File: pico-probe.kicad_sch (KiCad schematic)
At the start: 36 parts, among them J1 Conn_01x04, J2 USB_C_Receptacle_USB2.0, J3 Conn_01x05, SW1 SW_Push, U1 RP2040, U3 USBLC6-4SC6, U4 SPX1117-3.3, U5 W25Q16JVSS, Y1 Crystal_GND24

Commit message: 布线
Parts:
- added D2, D5: ESD5341, KisonNew:esd5341, symbol KisonNew:ESD5341
- C12, C13: LCSC C1648 -> C1554
- C15, C16: footprint Capacitor_SMD:C_0805_2012Metric -> Capacitor_SMD:C_0603_1608Metric; LCSC C15850 -> C19702; Price 0.08 -> 0.04
- C3, C5: LCSC C15849 -> C52923
- R3, R5: LCSC (none) -> C11702
- R6, R7: LCSC C325524 -> C25905
- Y1: LCSC (none) -> C9002
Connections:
- net EXT_5V is gone; now on net +5V: JP1.3 (B)
- net GND: now also D2.2 (A2), D5.2 (A2)
- net GPIO4: now also D5.1 (A1)
- net GPIO5: now also D2.1 (A1)
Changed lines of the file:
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@@
+    (effects (font (size 1.27 1.27)) (justify right bottom))
+  )
+  (label "TX" (at 221.234 120.396 180)
     (effects (font (size 1.27 1.27)) (justify right bottom))
   )
@@
     (effects (font (size 1.27 1.27)) (justify right bottom))
   )
+  (label "VSYS" (at 230.378 148.971 0)
+    (effects (font (size 1.27 1.27)) (justify left bottom))
+  )
   (label "GPIO18" (at 143.129 118.745 180)
     (effects (font (size 1.27 1.27)) (justify right bottom))
@@
   (label "GPIO12" (at 143.129 103.505 180)
     (effects (font (size 1.27 1.27)) (justify right bottom))
-  )
-  (label "EXT_5V" (at 230.378 148.971 0)
-    (effects (font (size 1.27 1.27)) (justify left bottom))
   )
   (label "QSPI_SD3" (at 281.051 100.203 180)
@@
   )
   (label "GPIO6" (at 143.129 88.265 180)
+    (effects (font (size 1.27 1.27)) (justify right bottom))
+  )
+  (label "RX" (at 221.615 129.286 180)
     (effects (font (size 1.27 1.27)) (justify right bottom))
   )
@@
       (effects (font (size 1.27 1.27)) (justify left))
     )
-    (property "Footprint" "Capacitor_SMD:C_0805_2012Metric" (id 2) (at 59.9948 187.96 0)
+    (property "Footprint" "Capacitor_SMD:C_0603_1608Metric" (id 2) (at 59.9948 187.96 0)
       (effects (font (size 1.27 1.27)) hide)
     )
@@
       (effects (font (size 1.27 1.27)) hide)
     )
-    (property "LCSC" "C15850" (id 4) (at 60.96 184.15 0)
-      (effects (font (size 1.27 1.27)) hide)
-    )
-    (property "Price" "0.08" (id 5) (at 60.96 184.15 0)
+    (property "LCSC" "C19702" (id 4) (at 60.96 184.15 0)
+      (effects (font (size 1.27 1.27)) hide)
+    )
+    (property "Price" "0.04" (id 5) (at 60.96 184.15 0)
       (effects (font (size 1.27 1.27)) hide)
     )
@@
       (effects (font (size 1.27 1.27)) hide)
     )
+    (property "LCSC" "C11702" (id 4) (at 257.429 41.529 0)
+      (effects (font (size 1.27 1.27)) hide)
+    )
     (pin "1")
     (pin "2")
@@
     )
     (property "Datasheet" "~" (id 3) (at 221.361 92.583 0)
+      (effects (font (size 1.27 1.27)) hide)
+    )
+    (property "LCSC" "C11702" (id 4) (at 221.361 92.583 0)
       (effects (font (size 1.27 1.27)) hide)
     )
@@
       (effects (font (size 1.27 1.27)) hide)
     )
-    (property "LCSC" "C1648" (id 4) (at 224.409 41.529 0)
+    (property "LCSC" "C1554" (id 4) (at 224.409 41.529 0)
       (effects (font (size 1.27 1.27)) hide)
     )
@@
     (pin "1")
   )
+  (symbol (lib_id "power:GND") (at 229.235 129.286 90) (unit 1)
+    (in_bom yes) (on_board yes) (fields_autoplaced)
+    (property "Reference" "#PWR0119" (id 0) (at 235.585 129.286 0)
+      (effects (font (size 1.27 1.27)) hide)
+    )
+    (property "Value" "GND" (id 1) (at 232.41 129.7198 90)
+      (effects (font (size 1.27 1.27)) (justify right))
+    )
+    (property "Footprint" "" (id 2) (at 229.235 129.286 0)
+      (effects (font (size 1.27 1.27)) hide)
+    )
+    (property "Datasheet" "" (id 3) (at 229.235 129.286 0)
+      (effects (font (size 1.27 1.27)) hide)
+    )
+    (pin "1")
+  )
+  (symbol (lib_id "power:GND") (at 228.854 120.396 90) (unit 1)
+    (in_bom yes) (on_board yes) (fields_autoplaced)
+    (property "Reference" "#PWR0118" (id 0) (at 235.204 120.396 0)
+      (effects (font (size 1.27 1.27)) hide)
+    )
+    (property "Value" "GND" (id 1) (at 232.029 120.8298 90)
+      (effects (font (size 1.27 1.27)) (justify right))
+    )
+    (property "Footprint" "" (id 2) (at 228.854 120.396 0)
+      (effects (font (size 1.27 1.27)) hide)
+    )
+    (property "Datasheet" "" (id 3) (at 228.854 120.396 0)
+      (effects (font (size 1.27 1.27)) hide)
+    )
+    (pin "1")
+  )
   (symbol (lib_id "Device:C") (at 121.539 42.545 0) (unit 1)
     (in_bom yes) (on_board yes)
@@
       (effects (font (size 1.27 1.27)) hide)
     )
-    (property "LCSC" "C15849" (id 4) (at 121.539 42.545 0)
+    (property "LCSC" "C52923" (id 4) (at 121.539 42.545 0)
       (effects (font (size 1.27 1.27)) hide)
     )
@@
       (effects (font (size 1.27 1.27)) hide)
     )
+    (property "LCSC" "C9002" (id 4) (at 239.649 36.449 0)
+      (effects (font (size 1.27 1.27)) hide)
+    )
     (pin "1")
     (pin "2")
@@
       (effects (font (size 1.27 1.27)) hide)
     )
-    (property "LCSC" "C15849" (id 4) (at 66.929 42.545 0)
+    (property "LCSC" "C52923" (id 4) (at 66.929 42.545 0)
       (effects (font (size 1.27 1.27)) hide)
     )
@@
       (effects (font (size 1.27 1.27)) hide)
     )
-    (property "LCSC" "C1648" (id 4) (at 224.409 31.369 0)
+    (property "LCSC" "C1554" (id 4) (at 224.409 31.369 0)
       (effects (font (size 1.27 1.27)) hide)
     )
@@
       (effects (font (size 1.27 1.27)) hide)
     )
-    (property "LCSC" "C325524" (id 4) (at 45.72 161.544 0)
+    (property "LCSC" "C25905" (id 4) (at 45.72 161.544 0)
       (effects (font (size 1.27 1.27)) hide)
     )
@@
       (effects (font (size 1.27 1.27)) hide)
     )
-    (property "LCSC" "C325524" (id 4) (at 45.72 159.004 0)
+    (property "LCSC" "C25905" (id 4) (at 45.72 159.004 0)
       (effects (font (size 1.27 1.27)) hide)
     )
@@
     )
     (pin "1")
+  )
+  (symbol (lib_id "KisonNew:ESD5341") (at 225.425 129.286 0) (unit 1)
+    (in_bom yes) (on_board yes) (fields_autoplaced)
+    (property "Reference" "D5" (id 0) (at 225.4885 124.3416 0))
+    (property "Value" "ESD5341" (id 1) (at 225.4885 126.8785 0))
+    (property "Footprint" "KisonNew:esd5341" (id 2) (at 225.425 122.936 0)
+      (effects (font (size 1.27 1.27)) hide)
+    )
+    (property "Datasheet" "" (id 3) (at 226.695 124.206 0)
+      (effects (font (size 1.27 1.27)) hide)
+    )
+    (property "LCSC" "C239773" (id 4) (at 225.425 129.286 0)
+      (effects (font (size 1.27 1.27)) hide)
+    )
+    (property "Price" "0.2" (id 5) (at 225.425 129.286 0)
+      (effects (font (size 1.27 1.27)) hide)
+    )
+    (pin "1")
+    (pin "2")
   )
   (symbol (lib_id "power:GND") (at 194.691 92.583 0) (unit 1)
@@
     (pin "1")
   )
+  (symbol (lib_id "KisonNew:ESD5341") (at 225.044 120.396 0) (unit 1)
+    (in_bom yes) (on_board yes) (fields_autoplaced)
+    (property "Reference" "D2" (id 0) (at 225.1075 115.4516 0))
+    (property "Value" "ESD5341" (id 1) (at 225.1075 117.9885 0))
+    (property "Footprint" "KisonNew:esd5341" (id 2) (at 225.044 114.046 0)
+      (effects (font (size 1.27 1.27)) hide)
+    )
+    (property "Datasheet" "" (id 3) (at 226.314 115.316 0)
+      (effects (font (size 1.27 1.27)) hide)
+    )
+    (property "LCSC" "C239773" (id 4) (at 225.044 120.396 0)
+      (effects (font (size 1.27 1.27)) hide)
+    )
+    (property "Price" "0.2" (id 5) (at 225.044 120.396 0)
+      (effects (font (size 1.27 1.27)) hide)
+    )
+    (pin "1")
+    (pin "2")
+  )
   (symbol (lib_id "power:+1V1") (at 75.819 20.955 0) (unit 1)
     (in_bom yes) (on_board yes)
@@
       (effects (font (size 1.27 1.27)) (justify left))
     )
-    (property "Footprint" "Capacitor_SMD:C_0805_2012Metric" (id 2) (at 77.1652 187.96 0)
+    (property "Footprint" "Capacitor_SMD:C_0603_1608Metric" (id 2) (at 77.1652 187.96 0)
       (effects (font (size 1.27 1.27)) hide)
     )
@@
       (effects (font (size 1.27 1.27)) hide)
     )
-    (property "LCSC" "C15850" (id 4) (at 76.2 184.15 0)
-      (effects (font (size 1.27 1.27)) hide)
-    )
-    (property "Price" "0.08" (id 5) (at 76.2 184.15 0)
+    (property "LCSC" "C19702" (id 4) (at 76.2 184.15 0)
+      (effects (font (size 1.27 1.27)) hide)
+    )
+    (property "Price" "0.04" (id 5) (at 76.2 184.15 0)
       (effects (font (size 1.27 1.27)) hide)
     )
@@
       (reference "#PWR0117") (unit 1) (value "GND") (footprint "")
     )
+    (path "/5be2a7ef-6d75-469c-9372-d3ffb1deb597"
+      (reference "#PWR0118") (unit 1) (value "GND") (footprint "")
+    )
+    (path "/5b45f8dc-bdc9-483f-a370-b95cb3c66794"
+      (reference "#PWR0119") (unit 1) (value "GND") (footprint "")
+    )
     (path "/775ab88d-bcfe-4114-9420-f4fd8ff148c3"
       (reference "#PWR0120") (unit 1) (value "GND") (footprint "")
@@
     )
     (path "/0516868f-abb8-4b83-8e2d-2d322e9f7b87"
-      (reference "C15") (unit 1) (value "10uf") (footprint "Capacitor_SMD:C_0805_2012Metric")
+      (reference "C15") (unit 1) (value "10uf") (footprint "Capacitor_SMD:C_0603_1608Metric")
     )
     (path "/f8ea8509-0869-4765-a579-07b13d0cb0fd"
-      (reference "C16") (unit 1) (value "10uf") (footprint "Capacitor_SMD:C_0805_2012Metric")
+      (reference "C16") (unit 1) (value "10uf") (footprint "Capacitor_SMD:C_0603_1608Metric")
     )
     (path "/99fe2f6d-1f82-4f84-a150-a09d92a8f576"
       (reference "D1") (unit 1) (value "D") (footprint "KisonNew:C8678")
     )
+    (path "/df9c2dea-53d2-468a-b74a-d1daef510987"
+      (reference "D2") (unit 1) (value "ESD5341") (footprint "KisonNew:esd5341")
+    )
     (path "/54bc26a8-1258-45ab-b9ed-89a95631aa30"
       (reference "D3") (unit 1) (value "ESD5341") (footprint "KisonNew:esd5341")
@@
       (reference "D4") (unit 1) (value "ESD5341") (footprint "KisonNew:esd5341")
     )
+    (path "/c2152c92-14f4-4079-9d64-d37e9be7e0d9"
+      (reference "D5") (unit 1) (value "ESD5341") (footprint "KisonNew:esd5341")
+    )
     (path "/6c900b51-bd89-4dac-8fad-0aea210c3a6d"

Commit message: 新布线
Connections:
- net DeviceVcc: now also J3.1 (Pin_1)
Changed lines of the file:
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@@
+    (effects (font (size 1.27 1.27)) (justify right bottom))
+  )
+  (label "DeviceVcc" (at 178.308 124.587 180)
     (effects (font (size 1.27 1.27)) (justify right bottom))
   )

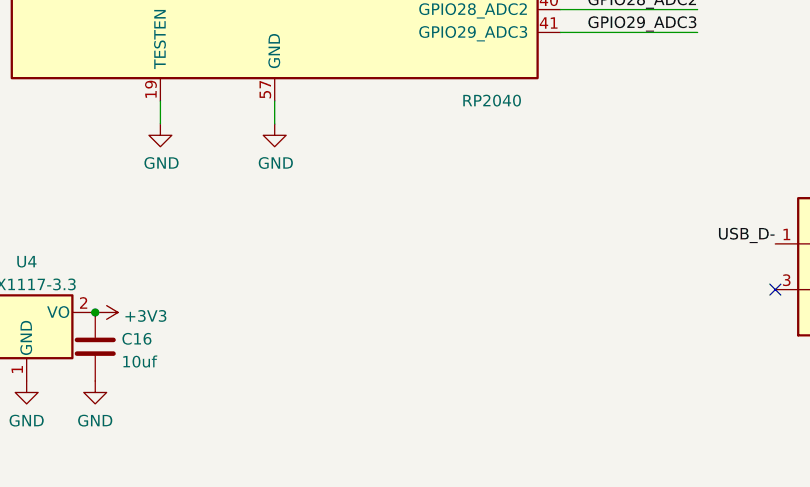
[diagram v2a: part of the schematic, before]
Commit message: 添加LED
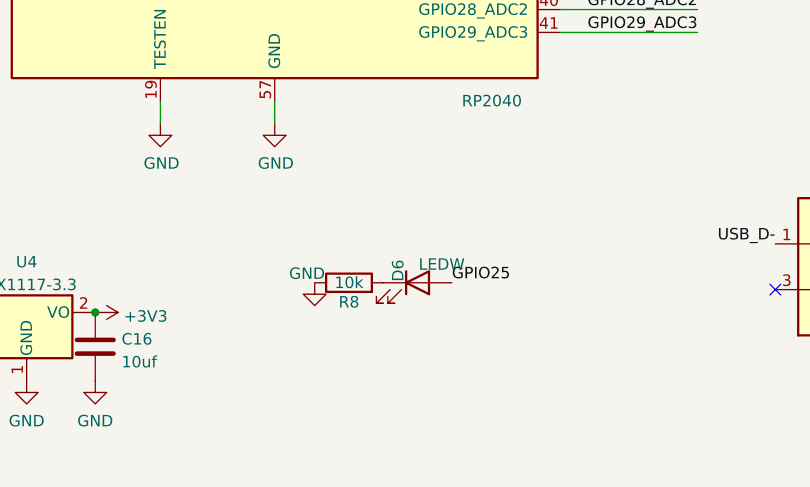
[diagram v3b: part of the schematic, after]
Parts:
- added D6: LEDW, LED_SMD:LED_0603_1608Metric, symbol Device:LED
- added R8: 10k, Resistor_SMD:R_0402_1005Metric, symbol Device:R
- C15, C16: Price 0.04 -> (none)
- D2, D3, D4, D5: Price 0.2 -> (none)
- U4: Price 0.76 -> (none)
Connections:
- net GND: now also R8.1
- net GPIO25: now also D6.2 (A)
- new net: D6.1 (K), R8.2
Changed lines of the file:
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@@
     (effects (font (size 1.27 1.27)) (justify right bottom))
+  )
+  (label "GPIO25" (at 115.824 177.038 0)
+    (effects (font (size 1.27 1.27)) (justify left bottom))
   )
   (label "SWD" (at 50.419 140.335 0)
@@
       (effects (font (size 1.27 1.27)) hide)
     )
-    (property "Price" "0.2" (id 5) (at 179.451 150.114 0)
+    (property "Price" "" (id 5) (at 179.451 150.114 0)
       (effects (font (size 1.27 1.27)) hide)
     )
@@
       (effects (font (size 1.27 1.27)) hide)
     )
-    (property "Price" "0.04" (id 5) (at 60.96 184.15 0)
+    (property "Price" "" (id 5) (at 60.96 184.15 0)
       (effects (font (size 1.27 1.27)) hide)
     )
@@
     (pin "2")
   )
+  (symbol (lib_id "Device:R") (at 104.394 177.038 90) (unit 1)
+    (in_bom yes) (on_board yes)
+    (property "Reference" "R8" (id 0) (at 104.394 179.197 90))
+    (property "Value" "10k" (id 1) (at 104.394 177.038 90))
+    (property "Footprint" "Resistor_SMD:R_0402_1005Metric" (id 2) (at 104.394 178.816 90)
+      (effects (font (size 1.27 1.27)) hide)
+    )
+    (property "Datasheet" "~" (id 3) (at 104.394 177.038 0)
+      (effects (font (size 1.27 1.27)) hide)
+    )
+    (property "LCSC" "C25744" (id 4) (at 104.394 177.038 0)
+      (effects (font (size 1.27 1.27)) hide)
+    )
+    (property "Price" "" (id 5) (at 104.394 177.038 0)
+      (effects (font (size 1.27 1.27)) hide)
+    )
+    (pin "1")
+    (pin "2")
+  )
   (symbol (lib_id "Device:C") (at 132.969 27.305 0) (unit 1)
     (in_bom yes) (on_board yes)
@@
     )
     (property "Datasheet" "" (id 3) (at 60.96 180.34 0)
+      (effects (font (size 1.27 1.27)) hide)
+    )
+    (pin "1")
+  )
+  (symbol (lib_id "power:GND") (at 100.584 177.038 0) (unit 1)
+    (in_bom yes) (on_board yes)
+    (property "Reference" "#PWR0132" (id 0) (at 100.584 183.388 0)
+      (effects (font (size 1.27 1.27)) hide)
+    )
+    (property "Value" "GND" (id 1) (at 101.727 176.022 0)
+      (effects (font (size 1.27 1.27)) (justify right))
+    )
+    (property "Footprint" "" (id 2) (at 100.584 177.038 0)
+      (effects (font (size 1.27 1.27)) hide)
+    )
+    (property "Datasheet" "" (id 3) (at 100.584 177.038 0)
       (effects (font (size 1.27 1.27)) hide)
     )
@@
     (pin "5")
     (pin "6")
+  )
+  (symbol (lib_id "Device:LED") (at 112.014 177.038 0) (unit 1)
+    (in_bom yes) (on_board yes)
+    (property "Reference" "D6" (id 0) (at 109.855 176.911 90)
+      (effects (font (size 1.27 1.27)) (justify left))
+    )
+    (property "Value" "LEDW" (id 1) (at 112.1287 175.006 0)
+      (effects (font (size 1.27 1.27)) (justify left))
+    )
+    (property "Footprint" "LED_SMD:LED_0603_1608Metric" (id 2) (at 112.014 177.038 0)
+      (effects (font (size 1.27 1.27)) hide)
+    )
+    (property "Datasheet" "~" (id 3) (at 112.014 177.038 0)
+      (effects (font (size 1.27 1.27)) hide)
+    )
+    (property "LCSC" "C2290" (id 4) (at 112.014 177.038 0)
+      (effects (font (size 1.27 1.27)) hide)
+    )
+    (property "Price" "" (id 5) (at 112.014 177.038 0)
+      (effects (font (size 1.27 1.27)) hide)
+    )
+    (pin "1")
+    (pin "2")
   )
   (symbol (lib_id "Device:C") (at 55.499 27.305 0) (unit 1)
@@
       (effects (font (size 1.27 1.27)) hide)
     )
-    (property "Price" "0.2" (id 5) (at 179.07 141.224 0)
+    (property "Price" "" (id 5) (at 179.07 141.224 0)
       (effects (font (size 1.27 1.27)) hide)
     )
@@
       (effects (font (size 1.27 1.27)) hide)
     )
-    (property "Price" "0.2" (id 5) (at 225.425 129.286 0)
+    (property "Price" "" (id 5) (at 225.425 129.286 0)
       (effects (font (size 1.27 1.27)) hide)
     )
@@
       (effects (font (size 1.27 1.27)) hide)
     )
-    (property "Price" "0.2" (id 5) (at 225.044 120.396 0)
+    (property "Price" "" (id 5) (at 225.044 120.396 0)
       (effects (font (size 1.27 1.27)) hide)
     )
@@
       (effects (font (size 1.27 1.27)) hide)
     )
-    (property "Price" "0.04" (id 5) (at 76.2 184.15 0)
+    (property "Price" "" (id 5) (at 76.2 184.15 0)
       (effects (font (size 1.27 1.27)) hide)
     )
@@
       (effects (font (size 1.27 1.27)) hide)
     )
-    (property "Price" "0.76" (id 5) (at 68.58 180.34 0)
+    (property "Price" "" (id 5) (at 68.58 180.34 0)
       (effects (font (size 1.27 1.27)) hide)
     )
@@
       (reference "#PWR0131") (unit 1) (value "+3V3") (footprint "")
     )
+    (path "/2afba08e-6f69-43fc-889b-3f73a553e959"
+      (reference "#PWR0132") (unit 1) (value "GND") (footprint "")
+    )
     (path "/4aadfbdf-7f43-471a-9022-e0ae8efc63b6"
       (reference "#PWR0133") (unit 1) (value "GND") (footprint "")
@@
       (reference "D5") (unit 1) (value "ESD5341") (footprint "KisonNew:esd5341")
     )
+    (path "/3d4ce4e8-756a-48e3-8a36-bebd7d0ab027"
+      (reference "D6") (unit 1) (value "LEDW") (footprint "LED_SMD:LED_0603_1608Metric")
+    )
     (path "/6c900b51-bd89-4dac-8fad-0aea210c3a6d"
       (reference "J1") (unit 1) (value "Conn_01x04") (footprint "Connector_PinHeader_2.54mm:PinHeader_1x04_P2.54mm_Vertical")
@@
       (reference "R7") (unit 1) (value "5.1k") (footprint "Resistor_SMD:R_0402_1005Metric")
     )
+    (path "/24ede718-9d9d-4bee-ac83-3d8dd69a7351"
+      (reference "R8") (unit 1) (value "10k") (footprint "Resistor_SMD:R_0402_1005Metric")
+    )
     (path "/cb5ffe9a-900b-4868-a3db-5c75dec9a0b2"
